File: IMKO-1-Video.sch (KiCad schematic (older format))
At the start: 30 parts, among them J9 CONN_VIDEO, U18 82S129, U19 74LS244, U20 74LS244, U21 74LS08, U22 74LS32, U23 74LS86, U24 74LS163, U25 74LS00, U26 74LS374, U8 SFF96364, X2 1MHz

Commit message: Added U13
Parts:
- added R27, R28, R29: 1k, symbol R
- added U13: 74LS374, symbol 74LS374
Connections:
- wire segments 192 -> 208
- no-connect marks 1 -> 3
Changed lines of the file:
@@
-EESchema Schematic File Version 2  date Fri 12 Oct 2012 09:40:08 PM EEST
+EESchema Schematic File Version 2  date Fri 12 Oct 2012 10:30:28 PM EEST
 LIBS:power
 LIBS:device
@@
 	7450 3950 7450 4000
 Wire Wire Line
-	1350 3500 1100 3500
-Wire Wire Line
-	1350 3600 1100 3600
+	1100 3500 3200 3500
+Wire Wire Line
+	1100 3600 3200 3600
 Wire Wire Line
 	1100 3700 3200 3700
 Wire Wire Line
-	1350 3800 1100 3800
+	1100 3800 3200 3800
 Wire Wire Line
 	1100 3900 3200 3900
@@
 	12450 2300 14200 2300
 Connection ~ 12450 1600
+$Comp
+L 74LS374 U13
+U 1 1 50788120
+P 2300 1900
+F 0 "U13" H 2300 1900 60  0000 C CNN
+F 1 "74LS374" H 2350 1550 60  0000 C CNN
+	1    2300 1900
+	1    0    0    -1
+$EndComp
+Wire Wire Line
+	1600 1400 1200 1400
+Text Label 1200 1400 0    60   ~ 0
+VID.D6
+Wire Wire Line
+	1600 1500 1200 1500
+Text Label 1200 1500 0    60   ~ 0
+VID.D4
+Wire Wire Line
+	1600 1600 1200 1600
+Text Label 1200 1600 0    60   ~ 0
+VID.D2
+Wire Wire Line
+	1200 2000 1600 2000
+Text Label 1200 2000 0    60   ~ 0
+VID.D5
+Wire Wire Line
+	1600 2100 1200 2100
+Text Label 1200 2100 0    60   ~ 0
+VID.D0
+Wire Wire Line
+	1600 1900 1200 1900
+Text Label 1200 1900 0    60   ~ 0
+VID.D3
+Wire Wire Line
+	1600 1800 1200 1800
+Text Label 1200 1800 0    60   ~ 0
+VID.D1
+$Comp
+L GND #PWR028
+U 1 1 50788AE6
+P 1550 2450
+F 0 "#PWR028" H 1550 2450 30  0001 C CNN
+F 1 "GND" H 1550 2380 30  0001 C CNN
+	1    1550 2450
+	1    0    0    -1
+$EndComp
+Wire Wire Line
+	1600 2400 1550 2400
+Wire Wire Line
+	1550 2400 1550 2450
+NoConn ~ 1600 1700
+NoConn ~ 3000 1700
+Text Label 1150 2300 0    60   ~ 0
+VID.LOAD
+Wire Wire Line
+	1150 2300 1600 2300
+$Comp
+L R R27
+U 1 1 50789045
+P 2250 4450
+F 0 "R27" V 2330 4450 50  0000 C CNN
+F 1 "1k" V 2250 4450 50  0000 C CNN
+	1    2250 4450
+	1    0    0    -1
+$EndComp
+Wire Wire Line
+	2250 4200 2250 3500
+Connection ~ 2250 3500
+$Comp
+L GND #PWR029
+U 1 1 50789220
+P 2250 4750
+F 0 "#PWR029" H 2250 4750 30  0001 C CNN
+F 1 "GND" H 2250 4680 30  0001 C CNN
+	1    2250 4750
+	1    0    0    -1
+$EndComp
+Wire Wire Line
+	2250 4750 2250 4700
+$Comp
+L R R28
+U 1 1 5078930C
+P 2450 4450
+F 0 "R28" V 2530 4450 50  0000 C CNN
+F 1 "1k" V 2450 4450 50  0000 C CNN
+	1    2450 4450
+	1    0    0    -1
+$EndComp
+Wire Wire Line
+	2450 3600 2450 4200
+Connection ~ 2450 3600
+$Comp
+L GND #PWR030
+U 1 1 507894ED
+P 2450 4750
+F 0 "#PWR030" H 2450 4750 30  0001 C CNN
+F 1 "GND" H 2450 4680 30  0001 C CNN
+	1    2450 4750
+	1    0    0    -1
+$EndComp
+Wire Wire Line
+	2450 4750 2450 4700
+$Comp
+L R R29
+U 1 1 507895DC
+P 2650 4450
+F 0 "R29" V 2730 4450 50  0000 C CNN
+F 1 "1k" V 2650 4450 50  0000 C CNN
+	1    2650 4450
+	1    0    0    -1
+$EndComp
+Wire Wire Line
+	2650 3800 2650 4200
+Connection ~ 2650 3800
+$Comp
+L GND #PWR031
+U 1 1 507897C3
+P 2650 4750
+F 0 "#PWR031" H 2650 4750 30  0001 C CNN
+F 1 "GND" H 2650 4680 30  0001 C CNN
+	1    2650 4750
+	1    0    0    -1
+$EndComp
+Wire Wire Line
+	2650 4750 2650 4700
 $EndSCHEMATC

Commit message: Added U9, U14
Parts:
- added R30, R31, R32, R33, R34: 1k, symbol R
- added U14: 74LS165, symbol 74LS165
- added U9: RO-3-2513, MODULE, symbol RO-3-2513
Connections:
- net labels added: CHR1, CHR2, CHR3, CHR4, CHR5, SFF.RO0, SFF.RO1, SFF.RO2, VID.SHIFT
- wire segments 208 -> 240
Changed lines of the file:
@@
-EESchema Schematic File Version 2  date Fri 12 Oct 2012 10:30:28 PM EEST
+EESchema Schematic File Version 2  date Sat 13 Oct 2012 12:28:12 AM EEST
 LIBS:power
 LIBS:device
@@
 LIBS:o_memory
 LIBS:SFF96364
+LIBS:RO-3-2513
 LIBS:IMKO-1-Video-cache
 EELAYER 27 0
@@
 Wire Wire Line
 	2650 4750 2650 4700
+$Comp
+L RO-3-2513 U9
+U 1 1 50789F2B
+P 19000 3850
+F 0 "U9" H 19000 3750 50  0000 C CNN
+F 1 "RO-3-2513" H 19000 3950 50  0000 C CNN
+F 2 "MODULE" H 19000 3850 50  0001 C CNN
+F 3 "DOCUMENTATION" H 19000 3600 50  0001 C CNN
+	1    19000 3850
+	1    0    0    -1
+$EndComp
+Wire Wire Line
+	16700 4150 17050 4150
+Wire Wire Line
+	16700 4250 17050 4250
+Wire Wire Line
+	16700 4350 17050 4350
+Text Label 16750 4150 0    60   ~ 0
+SFF.RO0
+Text Label 16750 4250 0    60   ~ 0
+SFF.RO1
+Text Label 16750 4350 0    60   ~ 0
+SFF.RO2
+Wire Wire Line
+	18200 3400 17800 3400
+Wire Wire Line
+	18200 3500 17800 3500
+Wire Wire Line
+	18200 3600 17800 3600
+Wire Wire Line
+	18200 3700 17800 3700
+Wire Wire Line
+	18200 3800 17800 3800
+Wire Wire Line
+	18200 3900 17800 3900
+Wire Wire Line
+	18200 4000 17800 4000
+Wire Wire Line
+	18200 4100 17800 4100
+Wire Wire Line
+	18200 4200 17800 4200
+Text Label 17800 3400 0    60   ~ 0
+SFF.RO0
+Text Label 17800 3500 0    60   ~ 0
+SFF.RO1
+Text Label 17800 3600 0    60   ~ 0
+SFF.RO2
+Text Label 6800 5050 0    60   ~ 0
+SFF.RO2
+Wire Wire Line
+	7200 5050 6800 5050
+$Comp
+L 74LS165 U14
+U 1 1 5078AAA1
+P 22150 3900
+F 0 "U14" H 22300 3850 60  0000 C CNN
+F 1 "74LS165" H 22300 3650 60  0000 C CNN
+	1    22150 3900
+	1    0    0    -1
+$EndComp
+Wire Wire Line
+	19800 3500 21450 3500
+Wire Wire Line
+	19800 3600 21450 3600
+Wire Wire Line
+	19800 3700 21450 3700
+Wire Wire Line
+	19800 3800 21450 3800
+Wire Wire Line
+	19800 3900 21450 3900
+Text Label 19850 3500 0    60   ~ 0
+CHR1
+Text Label 19850 3600 0    60   ~ 0
+CHR2
+Text Label 19850 3700 0    60   ~ 0
+CHR3
+Text Label 19850 3800 0    60   ~ 0
+CHR4
+Text Label 19850 3900 0    60   ~ 0
+CHR5
+Text Label 21050 4250 0    60   ~ 0
+VID.LOAD
+Wire Wire Line
+	21450 4250 21050 4250
+Wire Wire Line
+	21450 4400 21000 4400
+Text Label 21000 4400 0    60   ~ 0
+VID.SHIFT
+Text Label 7700 7700 0    60   ~ 0
+VID.SHIFT
+$Comp
+L GND #PWR032
+U 1 1 5078B3B5
+P 21400 4550
+F 0 "#PWR032" H 21400 4550 30  0001 C CNN
+F 1 "GND" H 21400 4480 30  0001 C CNN
+	1    21400 4550
+	1    0    0    -1
+$EndComp
+Wire Wire Line
+	21400 4550 21400 4500
+Wire Wire Line
+	21400 4500 21450 4500
+$Comp
+L R R30
+U 1 1 5078B6E4
+P 20200 3150
+F 0 "R30" V 20280 3150 50  0000 C CNN
+F 1 "1k" V 20200 3150 50  0000 C CNN
+	1    20200 3150
+	1    0    0    -1
+$EndComp
+Wire Wire Line
+	20200 3400 20200 3900
+Connection ~ 20200 3900
+$Comp
+L VCC #PWR033
+U 1 1 5078B840
+P 20200 2850
+F 0 "#PWR033" H 20200 2950 30  0001 C CNN
+F 1 "VCC" H 20200 2950 30  0000 C CNN
+	1    20200 2850
+	1    0    0    -1
+$EndComp
+Wire Wire Line
+	20200 2850 20200 2900
+$Comp
+L R R31
+U 1 1 5078B952
+P 20400 3150
+F 0 "R31" V 20480 3150 50  0000 C CNN
+F 1 "1k" V 20400 3150 50  0000 C CNN
+	1    20400 3150
+	1    0    0    -1
+$EndComp
+$Comp
+L VCC #PWR034
+U 1 1 5078B958
+P 20400 2850
+F 0 "#PWR034" H 20400 2950 30  0001 C CNN
+F 1 "VCC" H 20400 2950 30  0000 C CNN
+	1    20400 2850
+	1    0    0    -1
+$EndComp
+Wire Wire Line
+	20400 2850 20400 2900
+Connection ~ 20400 3800
+$Comp
+L R R32
+U 1 1 5078BA7D
+P 20600 3150
+F 0 "R32" V 20680 3150 50  0000 C CNN
+F 1 "1k" V 20600 3150 50  0000 C CNN
+	1    20600 3150
+	1    0    0    -1
+$EndComp
+$Comp
+L VCC #PWR035
+U 1 1 5078BA83
+P 20600 2850
+F 0 "#PWR035" H 20600 2950 30  0001 C CNN
+F 1 "VCC" H 20600 2950 30  0000 C CNN
+	1    20600 2850
+	1    0    0    -1
+$EndComp
+Wire Wire Line
+	20600 2850 20600 2900
+$Comp
+L R R33
+U 1 1 5078BA8A
+P 20800 3150
+F 0 "R33" V 20880 3150 50  0000 C CNN
+F 1 "1k" V 20800 3150 50  0000 C CNN
+	1    20800 3150
+	1    0    0    -1
+$EndComp
+$Comp
+L VCC #PWR036
+U 1 1 5078BA90
+P 20800 2850
+F 0 "#PWR036" H 20800 2950 30  0001 C CNN
+F 1 "VCC" H 20800 2950 30  0000 C CNN
+	1    20800 2850
+	1    0    0    -1
+$EndComp
+Wire Wire Line
+	20800 2850 20800 2900
+$Comp
+L R R34
+U 1 1 5078BA97
+P 21000 3150
+F 0 "R34" V 21080 3150 50  0000 C CNN
+F 1 "1k" V 21000 3150 50  0000 C CNN
+	1    21000 3150
+	1    0    0    -1
+$EndComp
+$Comp
+L VCC #PWR037
+U 1 1 5078BA9D
+P 21000 2850
+F 0 "#PWR037" H 21000 2950 30  0001 C CNN
+F 1 "VCC" H 21000 2950 30  0000 C CNN
+	1    21000 2850
+	1    0    0    -1
+$EndComp
+Wire Wire Line
+	21000 2850 21000 2900
+Wire Wire Line
+	20400 3800 20400 3400
+Wire Wire Line
+	20600 3400 20600 3700
+Connection ~ 20600 3700
+Wire Wire Line
+	20800 3400 20800 3600
+Connection ~ 20800 3600
+Wire Wire Line
+	21000 3400 21000 3500
+Connection ~ 21000 3500
 $EndSCHEMATC

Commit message: Added wiring
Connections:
- net labels added: CHR.A0, CHR.A1, CHR.A2, CHR.A3, CHR.A4, CHR.A5, CHR.D6, OUT.INH
- wire segments 240 -> 251
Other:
- note added: "TODO: Name"
- moved on the sheet: R22, U13, U8, X2
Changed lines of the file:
@@
-EESchema Schematic File Version 2  date Sat 13 Oct 2012 12:28:12 AM EEST
+EESchema Schematic File Version 2  date Sat 13 Oct 2012 01:02:51 AM EEST
 LIBS:power
 LIBS:device
@@
 L SFF96364 U8
 U 1 1 50771E3D
-P 15900 3550
-F 0 "U8" H 15900 3450 50  0000 C CNN
-F 1 "SFF96364" H 15900 3650 50  0000 C CNN
-F 2 "MODULE" H 15900 3550 50  0001 C CNN
-F 3 "DOCUMENTATION" H 15900 3550 50  0001 C CNN
-	1    15900 3550
+P 12900 3850
+F 0 "U8" H 12900 3750 50  0000 C CNN
+F 1 "SFF96364" H 12900 3950 50  0000 C CNN
+F 2 "MODULE" H 12900 3850 50  0001 C CNN
+F 3 "DOCUMENTATION" H 12900 3850 50  0001 C CNN
+	1    12900 3850
 	1    0    0    -1
 $EndComp
@@
 L CRYSTAL X2
 U 1 1 50771E58
-P 14750 4550
-F 0 "X2" V 14950 4450 60  0000 C CNN
-F 1 "1MHz" V 14550 4400 60  0000 C CNN
-	1    14750 4550
+P 11750 4850
+F 0 "X2" V 11950 4750 60  0000 C CNN
+F 1 "1MHz" V 11550 4700 60  0000 C CNN
+	1    11750 4850
 	0    -1   -1   0
 $EndComp
@@
 L R R22
 U 1 1 50771E7D
-P 14500 4550
-F 0 "R22" V 14580 4550 50  0000 C CNN
-F 1 "2M7" V 14500 4550 50  0000 C CNN
-	1    14500 4550
-	1    0    0    -1
-$EndComp
-Wire Wire Line
-	14500 4800 14500 4900
-Wire Wire Line
-	14500 4300 14500 4200
-Wire Wire Line
-	14500 4200 15000 4200
-Wire Wire Line
-	14750 4200 14750 4250
-Wire Wire Line
-	14500 4900 15000 4900
-Wire Wire Line
-	14750 4900 14750 4850
-Wire Wire Line
-	15000 4200 15000 4350
-Wire Wire Line
-	15000 4350 15100 4350
-Connection ~ 14750 4200
-Wire Wire Line
-	15000 4900 15000 4450
-Wire Wire Line
-	15000 4450 15100 4450
-Connection ~ 14750 4900
-Wire Wire Line
-	15100 3250 14650 3250
-Text Label 14650 3250 0    60   ~ 0
+P 11500 4850
+F 0 "R22" V 11580 4850 50  0000 C CNN
+F 1 "2M7" V 11500 4850 50  0000 C CNN
+	1    11500 4850
+	1    0    0    -1
+$EndComp
+Wire Wire Line
+	11500 5100 11500 5200
+Wire Wire Line
+	11500 4600 11500 4500
+Wire Wire Line
+	11500 4500 12000 4500
+Wire Wire Line
+	11750 4500 11750 4550
+Wire Wire Line
+	11500 5200 12000 5200
+Wire Wire Line
+	11750 5200 11750 5150
+Wire Wire Line
+	12000 4500 12000 4650
+Wire Wire Line
+	12000 4650 12100 4650
+Connection ~ 11750 4500
+Wire Wire Line
+	12000 5200 12000 4750
+Wire Wire Line
+	12000 4750 12100 4750
+Connection ~ 11750 5200
+Wire Wire Line
+	12100 3550 11650 3550
+Text Label 11650 3550 0    60   ~ 0
 SFF.PHI1
 Text Label 9800 7100 0    60   ~ 0
@@
 	14100 2100 14200 2100
 Wire Wire Line
-	16700 4550 17150 4550
-Text Label 16750 4550 0    60   ~ 0
+	13700 4850 14150 4850
+Text Label 13750 4850 0    60   ~ 0
 SFF.SYNC
 Text Label 10300 6950 0    60   ~ 0
@@
 	14250 7250 14250 7300
 Wire Wire Line
-	15100 3350 14650 3350
-Text Label 14650 3350 0    60   ~ 0
+	12100 3650 11650 3650
+Text Label 11650 3650 0    60   ~ 0
 ~SFF.INI
 Text Label 4650 7600 0    60   ~ 0
@@
 TODO: Name?
 Wire Wire Line
-	15100 3650 14650 3650
-Text Label 14650 3650 0    60   ~ 0
+	12100 3950 11650 3950
+Text Label 11650 3950 0    60   ~ 0
 SFF.W
 Text Label 6750 4550 0    60   ~ 0
@@
 L 74LS374 U13
 U 1 1 50788120
-P 2300 1900
-F 0 "U13" H 2300 1900 60  0000 C CNN
-F 1 "74LS374" H 2350 1550 60  0000 C CNN
-	1    2300 1900
-	1    0    0    -1
-$EndComp
-Wire Wire Line
-	1600 1400 1200 1400
-Text Label 1200 1400 0    60   ~ 0
+P 16150 4200
+F 0 "U13" H 16150 4200 60  0000 C CNN
+F 1 "74LS374" H 16200 3850 60  0000 C CNN
+	1    16150 4200
+	1    0    0    -1
+$EndComp
+Wire Wire Line
+	15450 3700 15050 3700
+Text Label 15050 3700 0    60   ~ 0
 VID.D6
 Wire Wire Line
-	1600 1500 1200 1500
-Text Label 1200 1500 0    60   ~ 0
+	15450 3800 15050 3800
+Text Label 15050 3800 0    60   ~ 0
 VID.D4
 Wire Wire Line
-	1600 1600 1200 1600
-Text Label 1200 1600 0    60   ~ 0
+	15450 3900 15050 3900
+Text Label 15050 3900 0    60   ~ 0
 VID.D2
 Wire Wire Line
-	1200 2000 1600 2000
-Text Label 1200 2000 0    60   ~ 0
+	15050 4300 15450 4300
+Text Label 15050 4300 0    60   ~ 0
 VID.D5
 Wire Wire Line
-	1600 2100 1200 2100
-Text Label 1200 2100 0    60   ~ 0
+	15450 4400 15050 4400
+Text Label 15050 4400 0    60   ~ 0
 VID.D0
 Wire Wire Line
-	1600 1900 1200 1900
-Text Label 1200 1900 0    60   ~ 0
+	15450 4200 15050 4200
+Text Label 15050 4200 0    60   ~ 0
 VID.D3
 Wire Wire Line
-	1600 1800 1200 1800
-Text Label 1200 1800 0    60   ~ 0
+	15450 4100 15050 4100
+Text Label 15050 4100 0    60   ~ 0
 VID.D1
 $Comp
 L GND #PWR028
 U 1 1 50788AE6
-P 1550 2450
-F 0 "#PWR028" H 1550 2450 30  0001 C CNN
-F 1 "GND" H 1550 2380 30  0001 C CNN
-	1    1550 2450
-	1    0    0    -1
-$EndComp
-Wire Wire Line
-	1600 2400 1550 2400
-Wire Wire Line
-	1550 2400 1550 2450
-NoConn ~ 1600 1700
-NoConn ~ 3000 1700
-Text Label 1150 2300 0    60   ~ 0
+P 15400 4750
+F 0 "#PWR028" H 15400 4750 30  0001 C CNN
+F 1 "GND" H 15400 4680 30  0001 C CNN
+	1    15400 4750
+	1    0    0    -1
+$EndComp
+Wire Wire Line
+	15450 4700 15400 4700
+Wire Wire Line
+	15400 4700 15400 4750
+NoConn ~ 15450 4000
+NoConn ~ 16850 4000
+Text Label 15000 4600 0    60   ~ 0
 VID.LOAD
 Wire Wire Line
-	1150 2300 1600 2300
+	15000 4600 15450 4600
 $Comp
 L R R27
@@
 $EndComp
 Wire Wire Line
-	16700 4150 17050 4150
-Wire Wire Line
-	16700 4250 17050 4250
-Wire Wire Line
-	16700 4350 17050 4350
-Text Label 16750 4150 0    60   ~ 0
+	13700 4450 14050 4450
+Wire Wire Line
+	13700 4550 14050 4550
+Wire Wire Line
+	13700 4650 14050 4650
+Text Label 13750 4450 0    60   ~ 0
 SFF.RO0
-Text Label 16750 4250 0    60   ~ 0
+Text Label 13750 4550 0    60   ~ 0
 SFF.RO1
-Text Label 16750 4350 0    60   ~ 0
+Text Label 13750 4650 0    60   ~ 0
 SFF.RO2
 Wire Wire Line
@@
 	21000 3400 21000 3500
 Connection ~ 21000 3500
+Wire Wire Line
+	16850 3700 17250 3700
+Wire Wire Line
+	16850 3800 17250 3800
+Wire Wire Line
+	16850 3900 17250 3900
+Wire Wire Line
+	16850 4100 17250 4100
+Wire Wire Line
+	16850 4200 17250 4200
+Wire Wire Line
+	16850 4300 17250 4300
+Wire Wire Line
+	16850 4400 17250 4400
+Text Label 16900 4400 0    60   ~ 0
+CHR.A0
+Text Label 17800 3700 0    60   ~ 0
+CHR.A0
+Text Label 16900 4100 0    60   ~ 0
+CHR.A1
+Text Label 17800 3800 0    60   ~ 0
+CHR.A1
+Text Label 16900 3900 0    60   ~ 0
+CHR.A2
+Text Label 17800 3900 0    60   ~ 0
+CHR.A2
+Text Label 16900 4200 0    60   ~ 0
+CHR.A3
+Text Label 17800 4000 0    60   ~ 0
+CHR.A3
+Text Label 17800 4100 0    60   ~ 0
+CHR.A4
+Text Label 16900 3800 0    60   ~ 0
+CHR.A4
+Text Label 16900 4300 0    60   ~ 0
+CHR.A5
+Text Label 17800 4200 0    60   ~ 0
+CHR.A5
+Wire Wire Line
+	18200 4400 17800 4400
+Text Label 17800 4400 0    60   ~ 0
+OUT.INH
+Text Label 15450 1750 0    60   ~ 0
+OUT.INH
+Wire Wire Line
+	15400 1750 15800 1750
+Text Label 10700 1500 0    60   ~ 0
+CHR.A5
+Wire Wire Line
+	11050 1500 10700 1500
+Text Label 16900 3700 0    60   ~ 0
+CHR.D6
+Text Notes 16900 3600 0    60   ~ 0
+TODO: Name
+Text Label 10700 1700 0    60   ~ 0
+CHR.D6
+Wire Wire Line
+	10700 1700 11050 1700
 $EndSCHEMATC

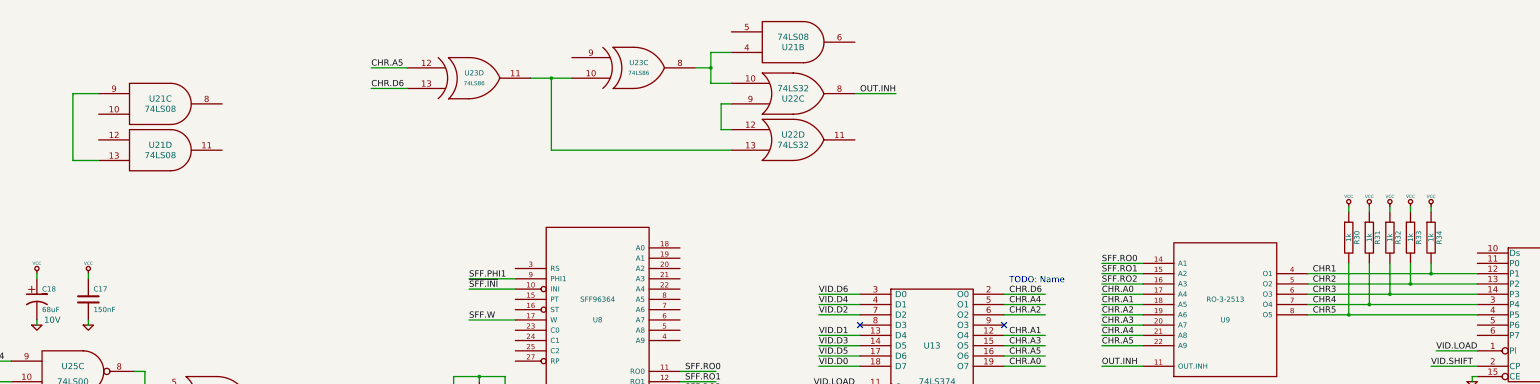
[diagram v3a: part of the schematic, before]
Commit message: Added missing U55
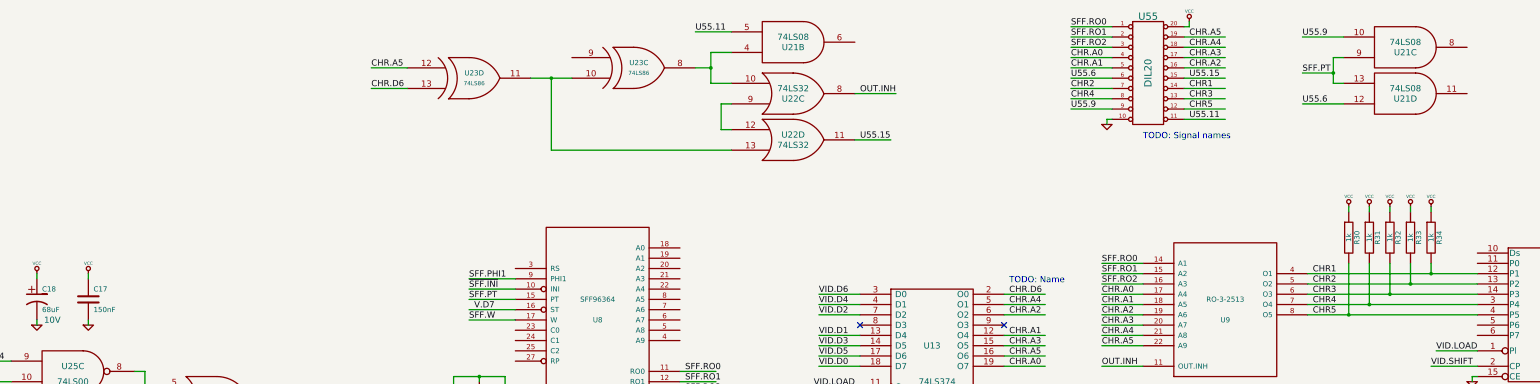
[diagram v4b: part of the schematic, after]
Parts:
- added U55: DIL20, symbol DIL20
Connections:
- net labels added: SFF.PT, U55.11, U55.15, U55.6, U55.9
- wire segments 251 -> 280
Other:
- note added: "TODO: Signal names"
- moved on the sheet: U21C, U21D
